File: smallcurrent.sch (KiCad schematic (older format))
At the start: 35 parts, among them J1 Screw_Terminal_01x01, J2 Screw_Terminal_01x01, J3 Screw_Terminal_01x01, J4 Screw_Terminal_01x01, J5 Conn_01x02, J6 Conn_01x04, SW1 OS203013MT8QN1-snapeda-OS2030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, SW2 OS203013MT8QN1, U1 MAX4239AUT, U2 LMV321, U3 STM809RWX6F, U4 MAX4239AUT

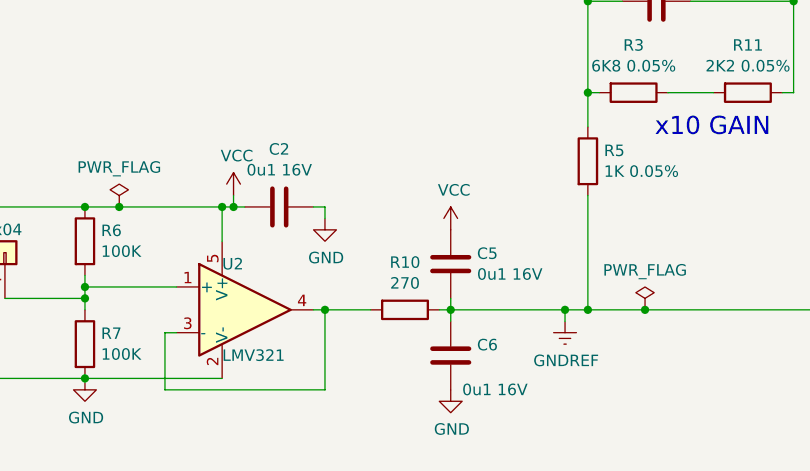
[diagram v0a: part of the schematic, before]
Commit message: Add footprint associations
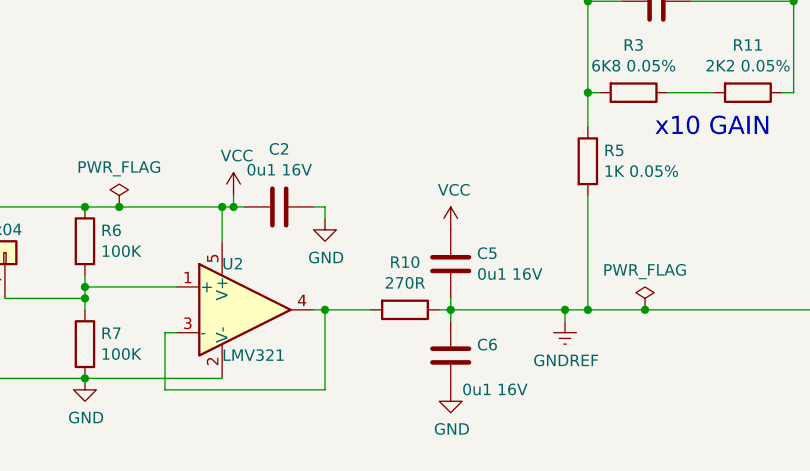
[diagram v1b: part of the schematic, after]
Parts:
- BC1: footprint (none) -> SnapEda:TE_5-1634503-1
- BT1: footprint (none) -> SnapEda:BAT_BS-7
- C1, C2, C3, C4, C5, C6: footprint (none) -> Capacitor_SMD:C_0603_1608Metric
- D1: footprint (none) -> LED_SMD:LED_0603_1608Metric
- J1, J2, J3, J4: footprint (none) -> homebrew:111-0703-001_BANANA_BINDING_POST
- J5: footprint (none) -> Connector_Hirose:Hirose_DF13-02P-1.25DSA_1x02_P1.25mm_Vertical
- J6: footprint (none) -> Connector_PinSocket_2.54mm:PinSocket_1x04_P2.54mm_Vertical
- R1: footprint (none) -> Resistor_SMD:R_2512_6332Metric
- R10: value 270 -> 270R; footprint (none) -> Resistor_SMD:R_0603_1608Metric
- R11, R12, R13, R14, R15, R2, R3, R4, R5, R6, R7: footprint (none) -> Resistor_SMD:R_0603_1608Metric
- R9: footprint (none) -> Resistor_SMD:R_0805_2012Metric
- SW1, SW2: footprint SW_OS203013MT8QN1 -> SnapEda:SW_OS203013MT8QN1
- U2: footprint (none) -> Package_TO_SOT_SMD:SOT-23-5
- U3: footprint (none) -> Package_TO_SOT_SMD:SOT-23
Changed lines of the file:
@@
 F 0 "BT1" H 1718 4346 50  0000 L CNN
 F 1 "Battery_Cell" H 1718 4255 50  0000 L CNN
-F 2 "" V 1600 4310 50  0001 C CNN
+F 2 "SnapEda:BAT_BS-7" V 1600 4310 50  0001 C CNN
 F 3 "~" V 1600 4310 50  0001 C CNN
 	1    1600 4250
@@
 F 0 "SW2" H 3280 3046 50  0000 L CNN
 F 1 "OS203013MT8QN1" H 3280 2955 50  0001 L CNN
-F 2 "SW_OS203013MT8QN1" H 2950 3000 50  0001 L BNN
+F 2 "SnapEda:SW_OS203013MT8QN1" H 2950 3000 50  0001 L BNN
 F 3 "" H 2950 3000 50  0001 L BNN
 F 4 "10.0mm" H 2950 3000 50  0001 L BNN "MAXIMUM_PACKAGE_HEIGHT"
@@
 F 0 "U3" H 2900 4265 50  0000 C CNN
 F 1 "STM809RWX6F" H 2900 4174 50  0000 C CNN
-F 2 "" H 2900 4300 50  0001 C CNN
+F 2 "Package_TO_SOT_SMD:SOT-23" H 2900 4300 50  0001 C CNN
 F 3 "" H 2900 4300 50  0001 C CNN
 	1    2900 4000
@@
 F 0 "R4" V 3343 4000 50  0000 C CNN
 F 1 "470R" V 3434 4000 50  0000 C CNN
-F 2 "" V 3480 4000 50  0001 C CNN
+F 2 "Resistor_SMD:R_0603_1608Metric" V 3480 4000 50  0001 C CNN
 F 3 "~" H 3550 4000 50  0001 C CNN
 	1    3550 4000
@@
 F 0 "D1" V 3789 4082 50  0000 R CNN
 F 1 "LED" V 3698 4082 50  0000 R CNN
-F 2 "" H 3750 4200 50  0001 C CNN
+F 2 "LED_SMD:LED_0603_1608Metric" H 3750 4200 50  0001 C CNN
 F 3 "~" H 3750 4200 50  0001 C CNN
 	1    3750 4200
@@
 F 0 "J6" V 4550 4050 50  0000 R CNN
 F 1 "Conn_01x04" V 4650 3950 50  0000 R CNN
-F 2 "" H 4550 3800 50  0001 C CNN
+F 2 "Connector_PinSocket_2.54mm:PinSocket_1x04_P2.54mm_Vertical" H 4550 3800 50  0001 C CNN
 F 3 "~" H 4550 3800 50  0001 C CNN
 	1    4550 3800
@@
 F 0 "R6" H 5170 3796 50  0000 L CNN
 F 1 "100K" H 5170 3705 50  0000 L CNN
-F 2 "" V 5030 3750 50  0001 C CNN
+F 2 "Resistor_SMD:R_0603_1608Metric" V 5030 3750 50  0001 C CNN
 F 3 "~" H 5100 3750 50  0001 C CNN
 	1    5100 3750
@@
 F 0 "R7" H 5170 4246 50  0000 L CNN
 F 1 "100K" H 5170 4155 50  0000 L CNN
-F 2 "" V 5030 4200 50  0001 C CNN
+F 2 "Resistor_SMD:R_0603_1608Metric" V 5030 4200 50  0001 C CNN
 F 3 "~" H 5100 4200 50  0001 C CNN
 	1    5100 4200
@@
 F 0 "U2" H 5700 4250 50  0000 L CNN
 F 1 "LMV321" H 5700 3850 50  0000 L CNN
-F 2 "" H 5800 4050 50  0001 L CNN
+F 2 "Package_TO_SOT_SMD:SOT-23-5" H 5800 4050 50  0001 L CNN
 F 3 "http://www.ti.com/lit/ds/symlink/lmv324.pdf" H 5800 4050 50  0001 C CNN
 	1    5800 4050
@@
 F 0 "C2" V 5698 3600 50  0000 C CNN
 F 1 "0u1 16V" V 5789 3600 50  0000 C CNN
-F 2 "" H 5988 3450 50  0001 C CNN
+F 2 "Capacitor_SMD:C_0603_1608Metric" H 5988 3450 50  0001 C CNN
 F 3 "~" H 5950 3600 50  0001 C CNN
 	1    5950 3600
@@
 P 6500 4050
 F 0 "R10" V 6293 4050 50  0000 C CNN
-F 1 "270" V 6384 4050 50  0000 C CNN
-F 2 "" V 6430 4050 50  0001 C CNN
+F 1 "270R" V 6384 4050 50  0000 C CNN
+F 2 "Resistor_SMD:R_0603_1608Metric" V 6430 4050 50  0001 C CNN
 F 3 "~" H 6500 4050 50  0001 C CNN
 	1    6500 4050
@@
 F 0 "C5" H 6585 3804 50  0000 R CNN
 F 1 "0u1 16V" H 6585 3895 50  0000 R CNN
-F 2 "" H 6738 3700 50  0001 C CNN
+F 2 "Capacitor_SMD:C_0603_1608Metric" H 6738 3700 50  0001 C CNN
 F 3 "~" H 6700 3850 50  0001 C CNN
 	1    6700 3850
@@
 F 0 "C6" H 6585 4204 50  0000 R CNN
 F 1 "0u1 16V" H 6650 4400 50  0000 R CNN
-F 2 "" H 6738 4100 50  0001 C CNN
+F 2 "Capacitor_SMD:C_0603_1608Metric" H 6738 4100 50  0001 C CNN
 F 3 "~" H 6700 4250 50  0001 C CNN
 	1    6700 4250
@@
 F 0 "J5" V 1564 3230 50  0000 L CNN
 F 1 "Conn_01x02" V 1700 2750 50  0000 L CNN
-F 2 "" H 1600 3150 50  0001 C CNN
+F 2 "Connector_Hirose:Hirose_DF13-02P-1.25DSA_1x02_P1.25mm_Vertical" H 1600 3150 50  0001 C CNN
 F 3 "~" H 1600 3150 50  0001 C CNN
 	1    1600 3150
@@
 F 0 "J2" H 2068 1775 50  0000 C CNN
 F 1 "Screw_Terminal_01x01" H 2068 1866 50  0000 C CNN
-F 2 "" H 2150 2000 50  0001 C CNN
+F 2 "homebrew:111-0703-001_BANANA_BINDING_POST" H 2150 2000 50  0001 C CNN
 F 3 "~" H 2150 2000 50  0001 C CNN
 	1    2150 2000
@@
 F 0 "J1" H 2068 1225 50  0000 C CNN
 F 1 "Screw_Terminal_01x01" H 2068 1316 50  0000 C CNN
-F 2 "" H 2150 1450 50  0001 C CNN
+F 2 "homebrew:111-0703-001_BANANA_BINDING_POST" H 2150 1450 50  0001 C CNN
 F 3 "~" H 2150 1450 50  0001 C CNN
 	1    2150 1450
@@
 F 0 "R2" H 3420 1796 50  0000 L CNN
 F 1 "10k 0.05%" H 3420 1705 50  0000 L CNN
-F 2 "" V 3280 1750 50  0001 C CNN
+F 2 "Resistor_SMD:R_0603_1608Metric" V 3280 1750 50  0001 C CNN
 F 3 "~" H 3350 1750 50  0001 C CNN
 	1    3350 1750
@@
 F 0 "SW1" V 5800 1200 50  0000 C CNN
 F 1 "OS203013MT8QN1-snapeda-OS203013" V 5174 950 50  0001 C CNN
-F 2 "SW_OS203013MT8QN1" H 5450 950 50  0001 L BNN
+F 2 "SnapEda:SW_OS203013MT8QN1" H 5450 950 50  0001 L BNN
 F 3 "" H 5450 950 50  0001 L BNN
 F 4 "10.0mm" H 5450 950 50  0001 L BNN "MAXIMUM_PACKAGE_HEIGHT"
@@
 F 0 "R1" H 4070 1796 50  0000 L CNN
 F 1 "0R01 0.1%" H 4070 1705 50  0000 L CNN
-F 2 "" V 3930 1750 50  0001 C CNN
+F 2 "Resistor_SMD:R_2512_6332Metric" V 3930 1750 50  0001 C CNN
 F 3 "~" H 4000 1750 50  0001 C CNN
 	1    4000 1750
@@
 F 0 "R9" H 4270 1446 50  0000 L CNN
 F 1 "10R 0.05%" H 4270 1355 50  0000 L CNN
-F 2 "" V 4130 1400 50  0001 C CNN
+F 2 "Resistor_SMD:R_0805_2012Metric" V 4130 1400 50  0001 C CNN
 F 3 "~" H 4200 1400 50  0001 C CNN
 	1    4200 1400
@@
 F 0 "R12" H 6270 1396 50  0000 L CNN
 F 1 "270R" H 6270 1305 50  0000 L CNN
-F 2 "" V 6130 1350 50  0001 C CNN
+F 2 "Resistor_SMD:R_0603_1608Metric" V 6130 1350 50  0001 C CNN
 F 3 "~" H 6200 1350 50  0001 C CNN
 	1    6200 1350
@@
 F 0 "C1" V 7048 1050 50  0000 C CNN
 F 1 "0u1 16V" V 7139 1050 50  0000 C CNN
-F 2 "" H 7338 900 50  0001 C CNN
+F 2 "Capacitor_SMD:C_0603_1608Metric" H 7338 900 50  0001 C CNN
 F 3 "~" H 7300 1050 50  0001 C CNN
 	1    7300 1050
@@
 F 0 "C3" V 7852 2700 50  0000 C CNN
 F 1 "10pF" V 7761 2700 50  0000 C CNN
-F 2 "" H 7638 2550 50  0001 C CNN
+F 2 "Capacitor_SMD:C_0603_1608Metric" H 7638 2550 50  0001 C CNN
 F 3 "~" H 7600 2700 50  0001 C CNN
 	1    7600 2700
@@
 F 0 "R3" V 7293 3100 50  0000 C CNN
 F 1 "6K8 0.05%" V 7384 3100 50  0000 C CNN
-F 2 "" V 7430 3100 50  0001 C CNN
+F 2 "Resistor_SMD:R_0603_1608Metric" V 7430 3100 50  0001 C CNN
 F 3 "~" H 7500 3100 50  0001 C CNN
 	1    7500 3100
@@
 F 0 "R11" V 7793 3100 50  0000 C CNN
 F 1 "2K2 0.05%" V 7884 3100 50  0000 C CNN
-F 2 "" V 7930 3100 50  0001 C CNN
+F 2 "Resistor_SMD:R_0603_1608Metric" V 7930 3100 50  0001 C CNN
 F 3 "~" H 8000 3100 50  0001 C CNN
 	1    8000 3100
@@
 F 0 "R5" H 7370 3446 50  0000 L CNN
 F 1 "1K 0.05%" H 7370 3355 50  0000 L CNN
-F 2 "" V 7230 3400 50  0001 C CNN
+F 2 "Resistor_SMD:R_0603_1608Metric" V 7230 3400 50  0001 C CNN
 F 3 "~" H 7300 3400 50  0001 C CNN
 	1    7300 3400
@@
 F 0 "C4" V 9402 2700 50  0000 C CNN
 F 1 "10pF" V 9311 2700 50  0000 C CNN
-F 2 "" H 9188 2550 50  0001 C CNN
+F 2 "Capacitor_SMD:C_0603_1608Metric" H 9188 2550 50  0001 C CNN
 F 3 "~" H 9150 2700 50  0001 C CNN
 	1    9150 2700
@@
 F 0 "R13" V 8843 3100 50  0000 C CNN
 F 1 "6K8 0.05%" V 8934 3100 50  0000 C CNN
-F 2 "" V 8980 3100 50  0001 C CNN
+F 2 "Resistor_SMD:R_0603_1608Metric" V 8980 3100 50  0001 C CNN
 F 3 "~" H 9050 3100 50  0001 C CNN
 	1    9050 3100
@@
 F 0 "R14" V 9343 3100 50  0000 C CNN
 F 1 "2K2 0.05%" V 9434 3100 50  0000 C CNN
-F 2 "" V 9480 3100 50  0001 C CNN
+F 2 "Resistor_SMD:R_0603_1608Metric" V 9480 3100 50  0001 C CNN
 F 3 "~" H 9550 3100 50  0001 C CNN
 	1    9550 3100
@@
 F 0 "R15" H 8920 3446 50  0000 L CNN
 F 1 "1K 0.05%" H 8920 3355 50  0000 L CNN
-F 2 "" V 8780 3400 50  0001 C CNN
+F 2 "Resistor_SMD:R_0603_1608Metric" V 8780 3400 50  0001 C CNN
 F 3 "~" H 8850 3400 50  0001 C CNN
 	1    8850 3400
@@
 F 0 "J3" H 11030 1792 50  0000 L CNN
 F 1 "Screw_Terminal_01x01" H 11030 1701 50  0000 L CNN
-F 2 "" H 10950 1750 50  0001 C CNN
+F 2 "homebrew:111-0703-001_BANANA_BINDING_POST" H 10950 1750 50  0001 C CNN
 F 3 "~" H 10950 1750 50  0001 C CNN
 	1    10950 1750
@@
 F 0 "J4" H 11080 3742 50  0000 L CNN
 F 1 "Screw_Terminal_01x01" H 11080 3651 50  0000 L CNN
-F 2 "" H 11000 3700 50  0001 C CNN
+F 2 "homebrew:111-0703-001_BANANA_BINDING_POST" H 11000 3700 50  0001 C CNN
 F 3 "~" H 11000 3700 50  0001 C CNN
 	1    11000 3700
@@
 F 0 "BC1" H 10278 2788 50  0000 C CNN
 F 1 "Conn_Coaxial" H 10278 2697 50  0000 C CNN
-F 2 "" H 10350 2550 50  0001 C CNN
+F 2 "SnapEda:TE_5-1634503-1" H 10350 2550 50  0001 C CNN
 F 3 " ~" H 10350 2550 50  0001 C CNN
 	1    10350 2550

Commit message: Start layout
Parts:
- J3, J4: footprint homebrew:111-0703-001_BANANA_BINDING_POST -> homebrew:CT2230-BANANA-JACK
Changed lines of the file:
@@
 	4450 4350 5100 4350
 Connection ~ 5100 4350
-Wire Wire Line
-	3050 3600 3450 3600
 Connection ~ 3050 3600
 NoConn ~ 2850 2600
@@
 F 0 "J3" H 11030 1792 50  0000 L CNN
 F 1 "Screw_Terminal_01x01" H 11030 1701 50  0000 L CNN
-F 2 "homebrew:111-0703-001_BANANA_BINDING_POST" H 10950 1750 50  0001 C CNN
+F 2 "homebrew:CT2230-BANANA-JACK" H 10950 1750 50  0001 C CNN
 F 3 "~" H 10950 1750 50  0001 C CNN
 	1    10950 1750
@@
 F 0 "J4" H 11080 3742 50  0000 L CNN
 F 1 "Screw_Terminal_01x01" H 11080 3651 50  0000 L CNN
-F 2 "homebrew:111-0703-001_BANANA_BINDING_POST" H 11000 3700 50  0001 C CNN
+F 2 "homebrew:CT2230-BANANA-JACK" H 11000 3700 50  0001 C CNN
 F 3 "~" H 11000 3700 50  0001 C CNN
 	1    11000 3700
@@
 	1    0    0    -1
 $EndComp
-Connection ~ 3450 3600
-Wire Wire Line
-	3450 3600 5100 3600
 Wire Wire Line
 	1600 4350 1300 4350
@@
 Wire Wire Line
 	7550 4050 7300 4050
+Wire Wire Line
+	3050 3600 5100 3600
 $EndSCHEMATC

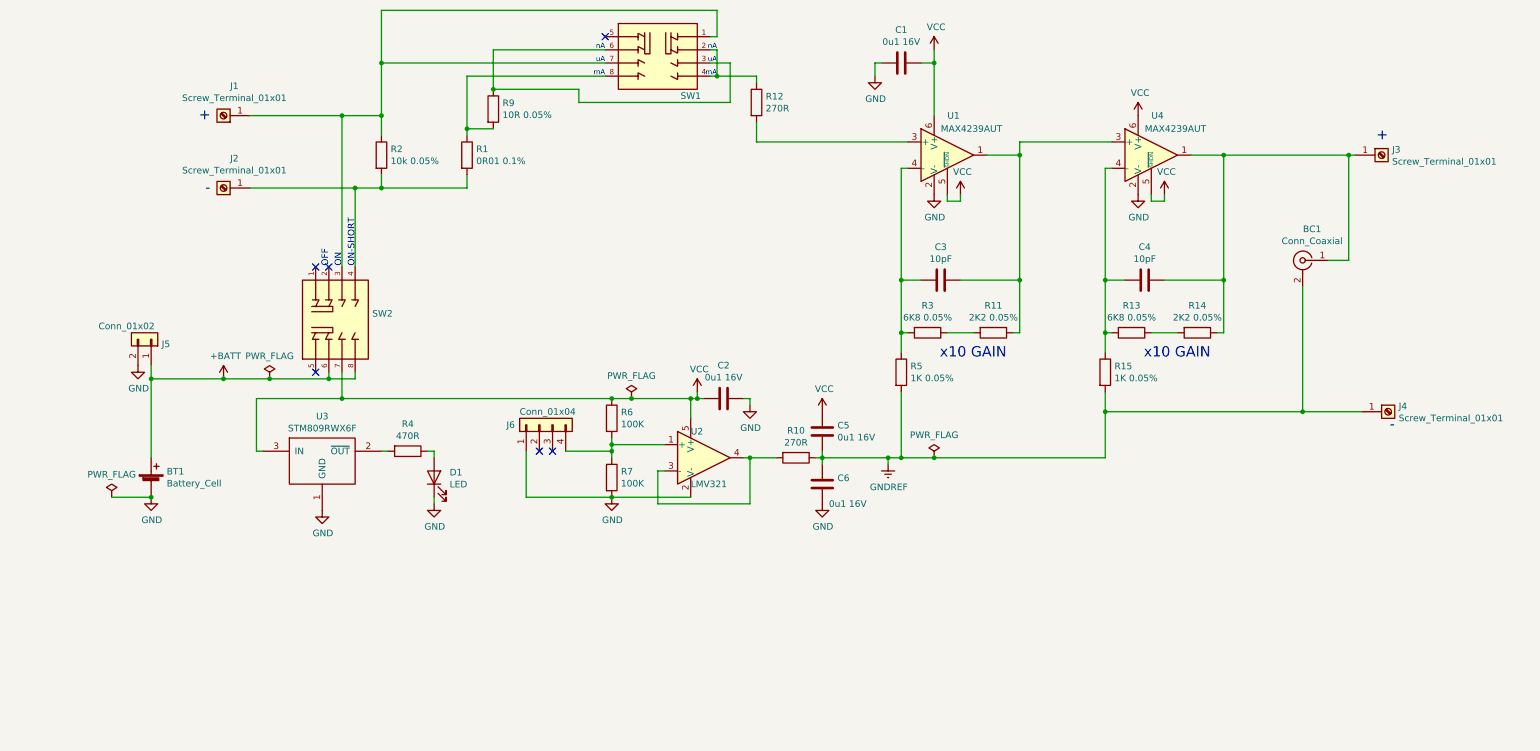
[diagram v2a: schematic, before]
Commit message: More layout: most parts in position
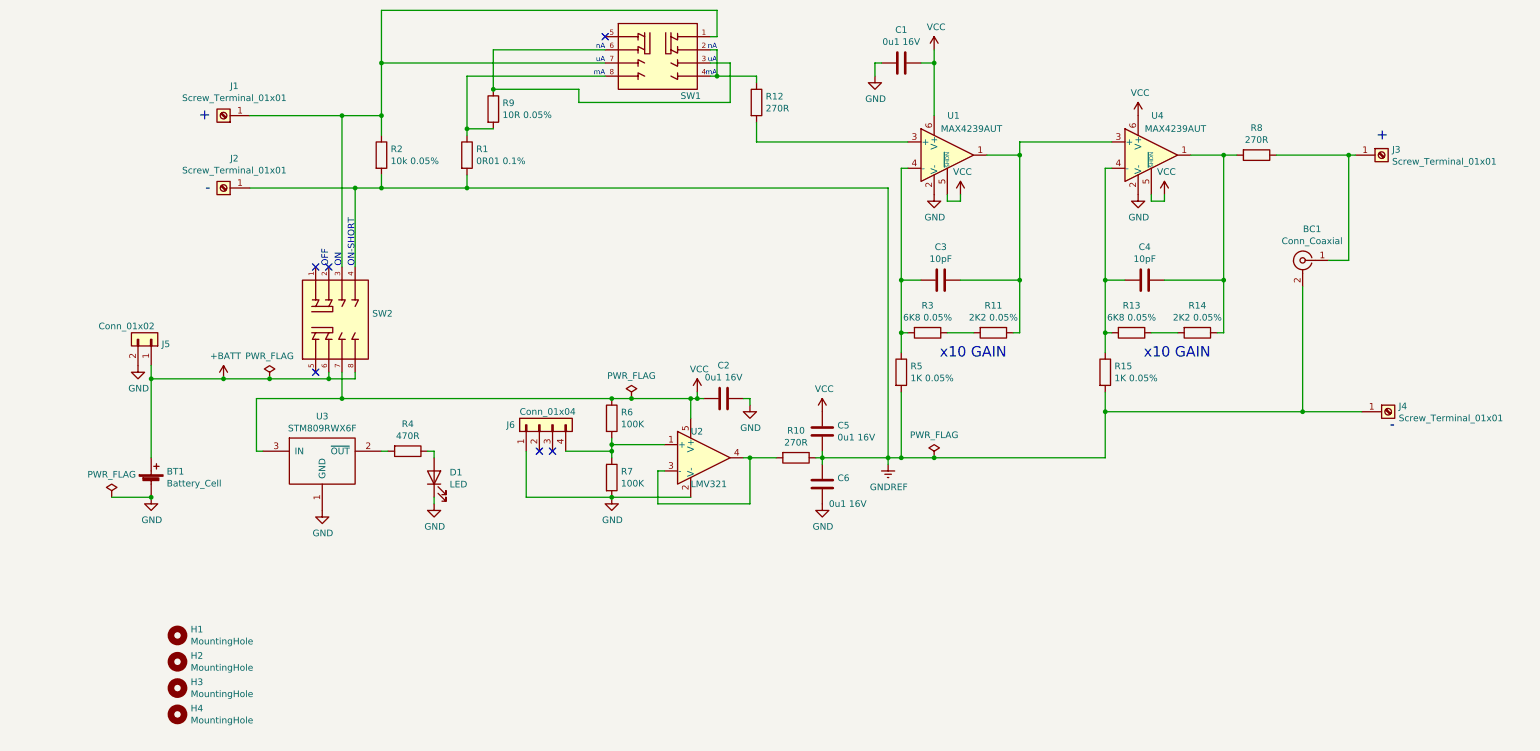
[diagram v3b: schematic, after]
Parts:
- added H1, H2, H3, H4: MountingHole, MountingHole:MountingHole_3.2mm_M3, symbol Mechanical:MountingHole
- added R8: 270R, Resistor_SMD:R_0603_1608Metric, symbol Device:R
- D1: footprint LED_SMD:LED_0603_1608Metric -> LED_THT:LED_D3.0mm
- R1: footprint Resistor_SMD:R_2512_6332Metric -> snapeda:Y14870R01000B9R
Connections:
- net GNDREF: now also J2.1 (Pin_1), R1.2, R2.2, SW2.4
- net at C4.2, R14.1, U4.1: now also R8.2; no longer BC1.1 (In), J3.1 (Pin_1)
- new net: BC1.1 (In), J3.1 (Pin_1), R8.1
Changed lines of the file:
@@
 F 0 "D1" V 3789 4082 50  0000 R CNN
 F 1 "LED" V 3698 4082 50  0000 R CNN
-F 2 "LED_SMD:LED_0603_1608Metric" H 3750 4200 50  0001 C CNN
+F 2 "LED_THT:LED_D3.0mm" H 3750 4200 50  0001 C CNN
 F 3 "~" H 3750 4200 50  0001 C CNN
 	1    3750 4200
@@
 F 0 "R1" H 4070 1796 50  0000 L CNN
 F 1 "0R01 0.1%" H 4070 1705 50  0000 L CNN
-F 2 "Resistor_SMD:R_2512_6332Metric" V 3930 1750 50  0001 C CNN
+F 2 "snapeda:Y14870R01000B9R" V 3930 1750 50  0001 C CNN
 F 3 "~" H 4000 1750 50  0001 C CNN
 	1    4000 1750
@@
 Wire Wire Line
 	10750 1750 10700 1750
-Connection ~ 9750 1750
 $Comp
 L Connector:Conn_Coaxial BC1
@@
 Wire Wire Line
 	10700 2550 10700 1750
-Connection ~ 10700 1750
-Wire Wire Line
-	10700 1750 9750 1750
 Wire Wire Line
 	10800 3700 10350 3700
@@
 Wire Wire Line
 	3050 3600 5100 3600
+$Comp
+L Mechanical:MountingHole H1
+U 1 1 5FBF0127
+P 1800 5400
+F 0 "H1" H 1900 5446 50  0000 L CNN
+F 1 "MountingHole" H 1900 5355 50  0000 L CNN
+F 2 "MountingHole:MountingHole_3.2mm_M3" H 1800 5400 50  0001 C CNN
+F 3 "~" H 1800 5400 50  0001 C CNN
+	1    1800 5400
+	1    0    0    -1
+$EndComp
+$Comp
+L Mechanical:MountingHole H2
+U 1 1 5FBF1185
+P 1800 5600
+F 0 "H2" H 1900 5646 50  0000 L CNN
+F 1 "MountingHole" H 1900 5555 50  0000 L CNN
+F 2 "MountingHole:MountingHole_3.2mm_M3" H 1800 5600 50  0001 C CNN
+F 3 "~" H 1800 5600 50  0001 C CNN
+	1    1800 5600
+	1    0    0    -1
+$EndComp
+$Comp
+L Mechanical:MountingHole H3
+U 1 1 5FBF1405
+P 1800 5800
+F 0 "H3" H 1900 5846 50  0000 L CNN
+F 1 "MountingHole" H 1900 5755 50  0000 L CNN
+F 2 "MountingHole:MountingHole_3.2mm_M3" H 1800 5800 50  0001 C CNN
+F 3 "~" H 1800 5800 50  0001 C CNN
+	1    1800 5800
+	1    0    0    -1
+$EndComp
+$Comp
+L Mechanical:MountingHole H4
+U 1 1 5FBF1655
+P 1800 6000
+F 0 "H4" H 1900 6046 50  0000 L CNN
+F 1 "MountingHole" H 1900 5955 50  0000 L CNN
+F 2 "MountingHole:MountingHole_3.2mm_M3" H 1800 6000 50  0001 C CNN
+F 3 "~" H 1800 6000 50  0001 C CNN
+	1    1800 6000
+	1    0    0    -1
+$EndComp
+Wire Wire Line
+	4000 2000 7200 2000
+Wire Wire Line
+	7200 2000 7200 4050
+Connection ~ 4000 2000
+$Comp
+L Device:R R8
+U 1 1 5FC22AB6
+P 10000 1750
+F 0 "R8" V 9793 1750 50  0000 C CNN
+F 1 "270R" V 9884 1750 50  0000 C CNN
+F 2 "Resistor_SMD:R_0603_1608Metric" V 9930 1750 50  0001 C CNN
+F 3 "~" H 10000 1750 50  0001 C CNN
+	1    10000 1750
+	0    1    1    0
+$EndComp
+Wire Wire Line
+	9750 1750 9850 1750
+Connection ~ 9750 1750
+Wire Wire Line
+	10150 1750 10700 1750
+Connection ~ 10700 1750
 $EndSCHEMATC

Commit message: Version 1.0
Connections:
- net at R8.2, U4.1: no longer C4.2, R14.1
- net at BC1.1 (In), J3.1 (Pin_1), R8.1: now also C4.2, R14.1
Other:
- moved on the sheet: BC1, BT1, C1, C2, C3, C4, C5, C6, D1, H1, H2, H3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
